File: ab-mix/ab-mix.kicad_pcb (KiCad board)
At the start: 2 copper layers, 110 x 84 mm, 70 parts, among them J1 IN, J2 Out, J3 Send1, J4 Return1, J5 Send2, J6 Return2, J7 Exp, Q1 J201, Q2 J201, Q3 Q_PNP_EBC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

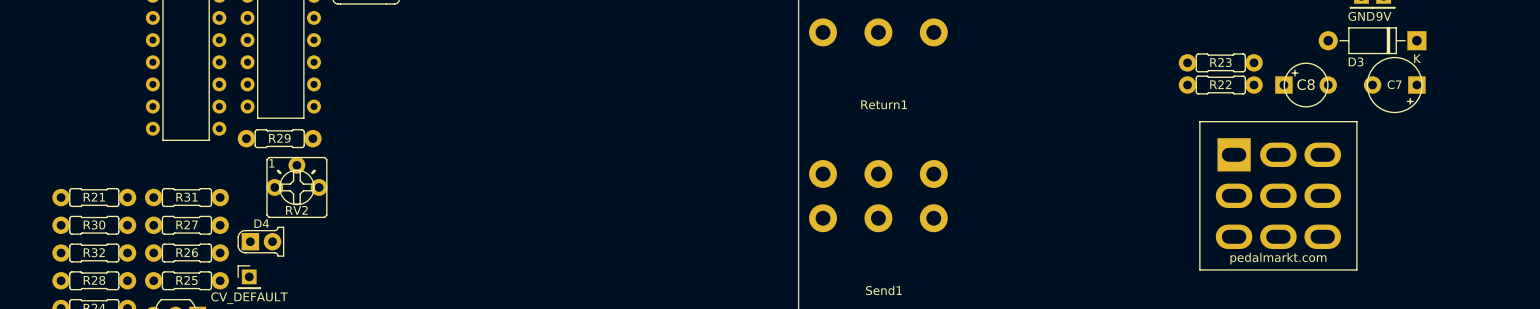
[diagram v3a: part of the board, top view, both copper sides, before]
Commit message: More power section
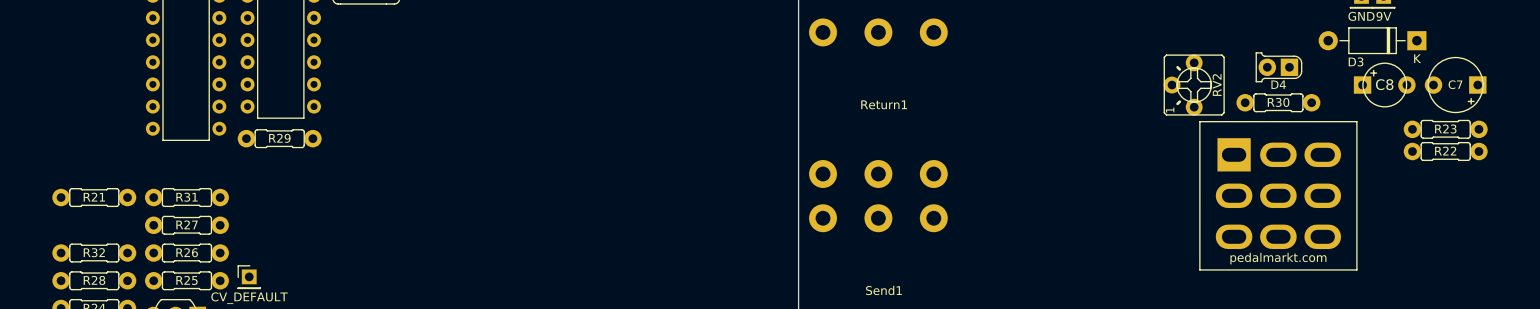
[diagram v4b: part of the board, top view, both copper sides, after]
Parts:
- moved R30 136.5 mm to (100.0, 89.3)
- moved D4 118.3 mm to (100.0, 85.3), turned to 180 degrees
- moved RV2 103.5 mm to (90.3, 87.3), turned to 90 degrees
- moved R22 26.9 mm to (119.2, 94.9)
- moved R23 26.9 mm to (119.2, 92.4)
- moved C8 9.02 mm to (112.2, 87.3)
- moved C7 6.98 mm to (120.3, 87.3)
- moved ? 1.02 mm to (100.0, 101.0)
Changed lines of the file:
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@@
   )
   (module "MBv3 enclosures:1590BB" (layer F.Cu)
-    (at 100 100 90)
+    (at 100 101.016 90)
     (fp_text reference "" (at 0 0 90) (layer F.SilkS)
       (effects (font (size 1.524 1.524) (thickness 0.15)))
@@
   )
   (module "MBv3 potentiometers:TRIM1" (layer F.Cu)
-    (at -12.507 99.041)
+    (at 90.348 87.3 90)
     (descr "<b>Bourns 3362p</b>\n<p>\n<a href=\"http://www.taydaelectronics.com/potentiometer-variable-resistors/cermet-potentiometers/3362p.html\">http://www.taydaelectronics.com/potentiometer-variable-resistors/cermet-potentiometers/3362p.html</a>")
-    (fp_text reference RV2 (at 0 2.667) (layer F.SilkS)
-      (effects (font (size 1 1) (thickness 0.15)))
-    )
-    (fp_text value 5K (at 0 2.7305) (layer F.SilkS) hide
-      (effects (font (size 1 1) (thickness 0.15)))
-    )
-    (fp_text user 1 (at -3.302 -2.159) (layer F.SilkS)
+    (fp_text reference RV2 (at 0 2.667 90) (layer F.SilkS)
+      (effects (font (size 1 1) (thickness 0.15)))
+    )
+    (fp_text value 5K (at 0 2.7305 90) (layer F.SilkS) hide
+      (effects (font (size 1 1) (thickness 0.15)))
+    )
+    (fp_text user 1 (at -3.302 -2.159 90) (layer F.SilkS)
       (effects (font (size 0.9652 0.9652) (thickness 0.08128)) (justify left bottom))
     )
@@
     (fp_line (start 3.175 -3.429) (end -3.175 -3.429) (layer F.SilkS) (width 0.1524))
     (fp_circle (center 0 0) (end 1.9715 0) (layer F.SilkS) (width 0.127))
-    (pad 3 thru_hole oval (at 2.54 0) (size 1.9304 1.9304) (drill 1) (layers *.Cu *.Mask)
+    (pad 3 thru_hole oval (at 2.54 0 90) (size 1.9304 1.9304) (drill 1) (layers *.Cu *.Mask)
       (net 68 "Net-(RV2-Pad3)"))
-    (pad 2 thru_hole oval (at 0 -2.54) (size 1.9304 1.9304) (drill 1) (layers *.Cu *.Mask)
+    (pad 2 thru_hole oval (at 0 -2.54 90) (size 1.9304 1.9304) (drill 1) (layers *.Cu *.Mask)
       (net 44 "Net-(J7-PadS)"))
-    (pad 1 thru_hole oval (at -2.54 0) (size 1.9304 1.9304) (drill 1) (layers *.Cu *.Mask)
+    (pad 1 thru_hole oval (at -2.54 0 90) (size 1.9304 1.9304) (drill 1) (layers *.Cu *.Mask)
       (net 7 GND))
   )
@@
   )
   (module "MBv3 resistors:0.3_22.B" (layer F.Cu)
-    (at -35.732201 103.378)
+    (at 100 89.332)
     (descr "0.3\"  (7.62mm) lead spacing, 1/4W (flat)")
     (fp_text reference R30 (at 0 0) (layer F.SilkS)
@@
   )
   (module "MBv3 resistors:0.3_22.B" (layer F.Cu)
-    (at 93.396 84.76)
+    (at 119.177 92.38)
     (descr "0.3\"  (7.62mm) lead spacing, 1/4W (flat)")
     (fp_text reference R23 (at 0 0) (layer F.SilkS)
@@
   )
   (module "MBv3 resistors:0.3_22.B" (layer F.Cu)
-    (at 93.396 87.3 180)
+    (at 119.177 94.92 180)
     (descr "0.3\"  (7.62mm) lead spacing, 1/4W (flat)")
     (fp_text reference R22 (at 0 0) (layer F.SilkS)
@@
   )
   (module "MBv3 diodes:3MM_1" (layer F.Cu)
-    (at -16.571699 105.2603)
+    (at 100 85.268 180)
     (fp_text reference D4 (at 0 -2.032) (layer F.SilkS)
       (effects (font (size 0.9652 0.9652) (thickness 0.08128)))
@@
     (fp_line (start -2.667 0.508) (end -2.667 -0.508) (layer F.SilkS) (width 0.127))
     (fp_arc (start -1.8415 0.444499) (end -1.778 1.27) (angle 90) (layer F.SilkS) (width 0.127))
-    (pad 1 thru_hole oval (at 1.27 0) (size 2 2) (drill 1) (layers *.Cu *.Mask)
+    (pad 1 thru_hole oval (at 1.27 0 180) (size 2 2) (drill 1) (layers *.Cu *.Mask)
       (net 21 "Net-(D4-Pad1)"))
-    (pad 2 thru_hole rect (at -1.27 0) (size 2 2) (drill 1) (layers *.Cu *.Mask)
+    (pad 2 thru_hole rect (at -1.27 0 180) (size 2 2) (drill 1) (layers *.Cu *.Mask)
       (net 13 +9V))
   )
@@
   )
   (module "MBv3 caps-elec:0504" (layer F.Cu)
-    (at 103.175 87.3)
+    (at 112.192 87.3)
     (descr "0.2\" (5.08mm) spacing")
     (fp_text reference C8 (at 0 0) (layer F.SilkS)
@@
   )
   (module "MBv3 caps-elec:0633" (layer F.Cu)
-    (at 113.335 87.3 180)
+    (at 120.32 87.3 180)
     (descr "0.2\" (5.08mm) spacing")
     (fp_text reference C7 (at 0 0) (layer F.SilkS)

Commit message: First two chips 😭
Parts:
- C1, C5, C6: footprint MBv3 caps-film:0.2%22.MED -> MBv3 caps-film:0.2%22.SML
- moved R15 242.4 mm to (123.9, 121.3)
- moved R12 225.8 mm to (110.2, 136.2), turned to 180 degrees
- moved R18 220.2 mm to (114.0, 129.7), turned to 270 degrees
- moved U1 214.6 mm to (107.7, 125.9), turned to 270 degrees
- moved U2 208.0 mm to (90.0, 122.9), turned to 90 degrees
- moved R8 198.5 mm to (123.9, 123.9)
- moved R16 198.0 mm to (81.1, 137.1), turned to 180 degrees
- moved R10 197.7 mm to (81.0, 128.7), turned to 180 degrees
- moved D1 197.3 mm to (100.0, 85.8)
- moved C6 197.0 mm to (100.1, 136.2), turned to 180 degrees
- moved R9 196.1 mm to (100.0, 89.8)
- moved R13 194.3 mm to (101.4, 139.0), turned to 180 degrees
- moved R19 193.8 mm to (83.6, 119.0), turned to 90 degrees
- moved H1 193.4 mm to (134.8, 123.4), turned to 180 degrees
- moved D2 192.1 mm to (123.9, 117.3), turned to 180 degrees
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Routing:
- net JACK_OUT: track 0.00 -> 193.7 mm
- net +9V: track 0.00 -> 158.0 mm
- net OUT: track 0.00 -> 157.2 mm
- net FX_RETURN2: track 0.00 -> 99.9 mm
- net Net-(H1-Pad1): track 0.00 -> 90.3 mm
- net IN: track 0.00 -> 87.6 mm
- net FX_RETURN1: track 0.00 -> 83.4 mm
- net Net-(R18-Pad1): track 0.00 -> 68.6 mm
- net Net-(R14-Pad1): track 0.00 -> 66.8 mm
- net Net-(C2-Pad1): track 0.00 -> 57.1 mm
- net +4V5: track 0.00 -> 50.2 mm, vias 0 -> 1
- net Net-(C3-Pad1): track 0.00 -> 42.1 mm
- net Net-(SW1-Pad5): track 0.00 -> 40.4 mm
- net GND: track 0.00 -> 39.1 mm, vias 0 -> 3
- net FX_SEND1: track 0.00 -> 36.6 mm
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- added copper zone on F.Cu, net +4V5
- added copper zone on B.Cu, net GND

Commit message: Tmp
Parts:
- RV3: value R_POT -> Volume
- moved R32 185.8 mm to (147.0, 72.8), turned to 90 degrees
- moved Q3 179.1 mm to (115.2, 109.9), turned to 90 degrees
- moved U3 171.5 mm to (120.7, 98.5)
- moved RV1 169.2 mm to (115.1, 101.0), turned to 270 degrees
- moved R21 165.1 mm to (110.7, 108.6), turned to 270 degrees
- moved C9 132.6 mm to (126.9, 92.4), turned to 90 degrees
- moved R28 111.3 mm to (75.5, 104.8), turned to 180 degrees
- moved R24 111.2 mm to (75.5, 110.7)
- moved R25 101.2 mm to (75.5, 99.1), turned to 180 degrees
- moved R26 100.7 mm to (75.5, 101.9), turned to 180 degrees
- moved R27 100.7 mm to (75.5, 107.7), turned to 180 degrees
- moved U4 0.28 mm to (81.8, 93.0)
- moved R19 0.25 mm to (83.4, 119.0)
- moved R20 0.25 mm to (86.5, 119.0)
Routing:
- net FX_SEND1: track 36.6 -> 93.2 mm
- net +9V: track 158.0 -> 214.5 mm
- net Net-(R24-Pad1): track 0.00 -> 29.6 mm
- net Net-(R30-Pad2): track 0.00 -> 25.6 mm
- net Net-(R27-Pad2): track 0.00 -> 20.6 mm
- net FLIP_OUT2: track 25.9 -> 45.9 mm
- net FLIP_OUT1: track 36.0 -> 50.4 mm
- net Net-(R25-Pad1): track 0.00 -> 11.7 mm
- net Net-(R26-Pad1): track 0.00 -> 10.7 mm
- net GND: track 39.1 -> 45.8 mm, vias 3 -> 4
- net MIXER_IN: track 0.00 -> 2.92 mm

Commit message: That LAST connection!
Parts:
- removed ?: , MBv3 enclosures:1590BB
- C2, C3: value .1u -> 1u
- C9: footprint MBv3 caps-film:0.2%22.LRG -> MBv3 caps-film:0.2%22.MED
- moved R31 151.0 mm to (125.7, 91.1), turned to 270 degrees
- moved R29 142.9 mm to (128.4, 91.1), turned to 270 degrees
- moved C9 25.9 mm to (142.9, 72.1), turned to 270 degrees
- moved R32 1.05 mm to (147.2, 71.8)
- moved Q3 0.51 mm to (115.2, 109.4)
- moved R21 0.51 mm to (110.7, 108.1)
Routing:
- net JACK_IN: track 12.9 -> 137.1 mm
- net FX_SEND2: track 35.1 -> 133.1 mm
- net GND: track 45.8 -> 138.0 mm
- net Net-(C9-Pad2): track 0.00 -> 68.4 mm
- net MIXER_IN: track 2.92 -> 67.8 mm
- net CV: track 0.00 -> 48.1 mm
- net CI: track 0.00 -> 40.4 mm
- net Net-(R29-Pad1): track 0.00 -> 24.5 mm
- net +9V: track 214.5 -> 236.0 mm
- net Net-(R21-Pad2): track 0.00 -> 21.3 mm
- net +4V5: track 50.2 -> 31.1 mm, vias 1 -> 0
- net FLIP_IN2: track 10.6 -> 24.9 mm
- net Net-(Q3-Pad2): track 0.00 -> 13.8 mm
- net Net-(Q3-Pad1): track 0.00 -> 6.34 mm
- net Net-(R32-Pad1): track 0.00 -> 5.50 mm
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
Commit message: Is it done?!?!?!
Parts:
- added ?: , MBv3 enclosures:1590BB, F.Cu at (100.0, 100.0)
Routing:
- net GND: track 138.0 -> 166.8 mm
- net Net-(R18-Pad1): track 68.6 -> 55.6 mm
- net CV: track 48.1 -> 57.0 mm
- net Net-(C5-Pad2): track 37.8 -> 33.2 mm
- net JACK_OUT: track 193.7 -> 197.7 mm
- net +4V5: track 31.1 -> 33.4 mm, vias 0 -> 2
- net CI: track 40.4 -> 41.6 mm
- net Net-(R24-Pad1): track 29.6 -> 30.4 mm
